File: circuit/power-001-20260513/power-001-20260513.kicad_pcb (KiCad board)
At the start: 2 copper layers, 68.4 x 46.4 mm, 46 parts, among them J2 +5V_{Line}, J3 Power, J4 Logic, J5 Sub_{Power}, J6 Sub_{Signal}, Q1 BSS138, Q2 PMOS, U1 OKL-T/6-W12N-C, U2 OKL-T/6-W12N-C, U3 AZ1084-3.3, U4 BP5293-33, U5 PIC12F683-xSN

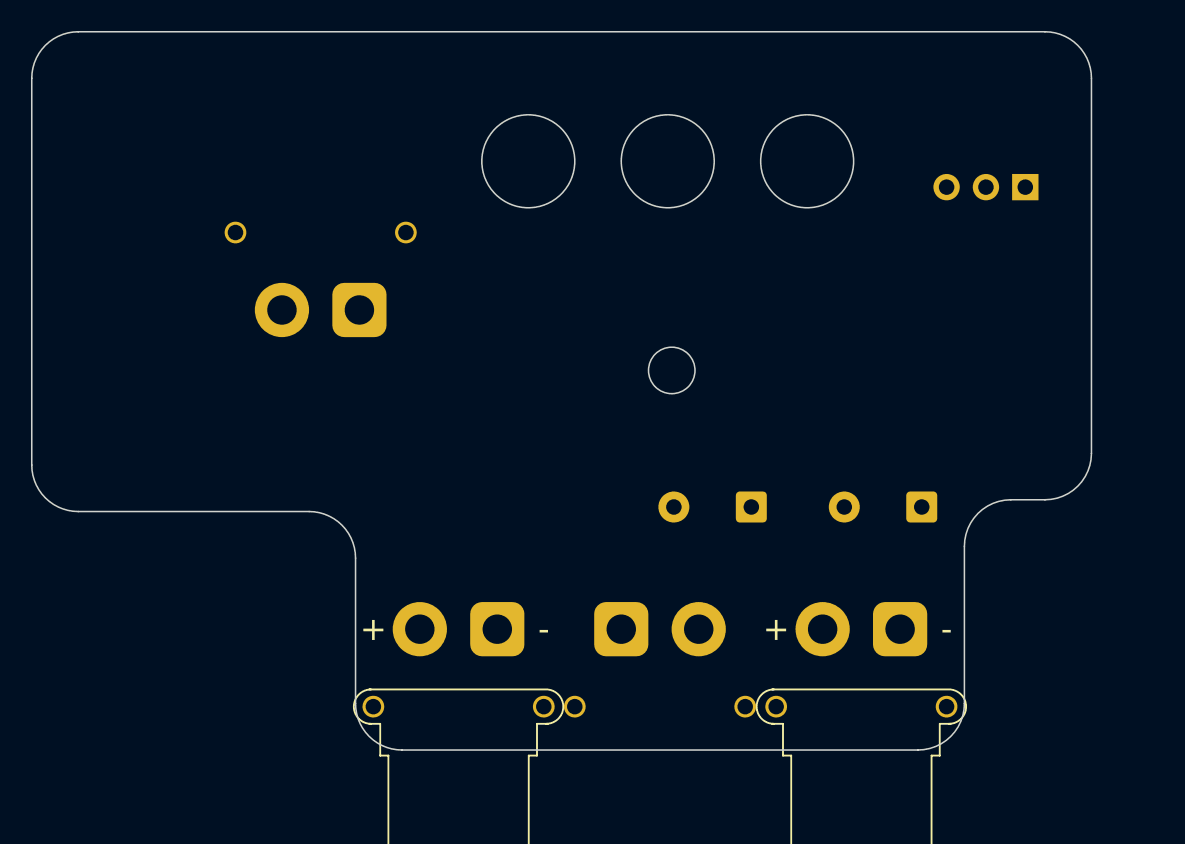
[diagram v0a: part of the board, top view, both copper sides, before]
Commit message: Update 電源基板のバッテリー接続口のフットプリントを作成＆紐づけ
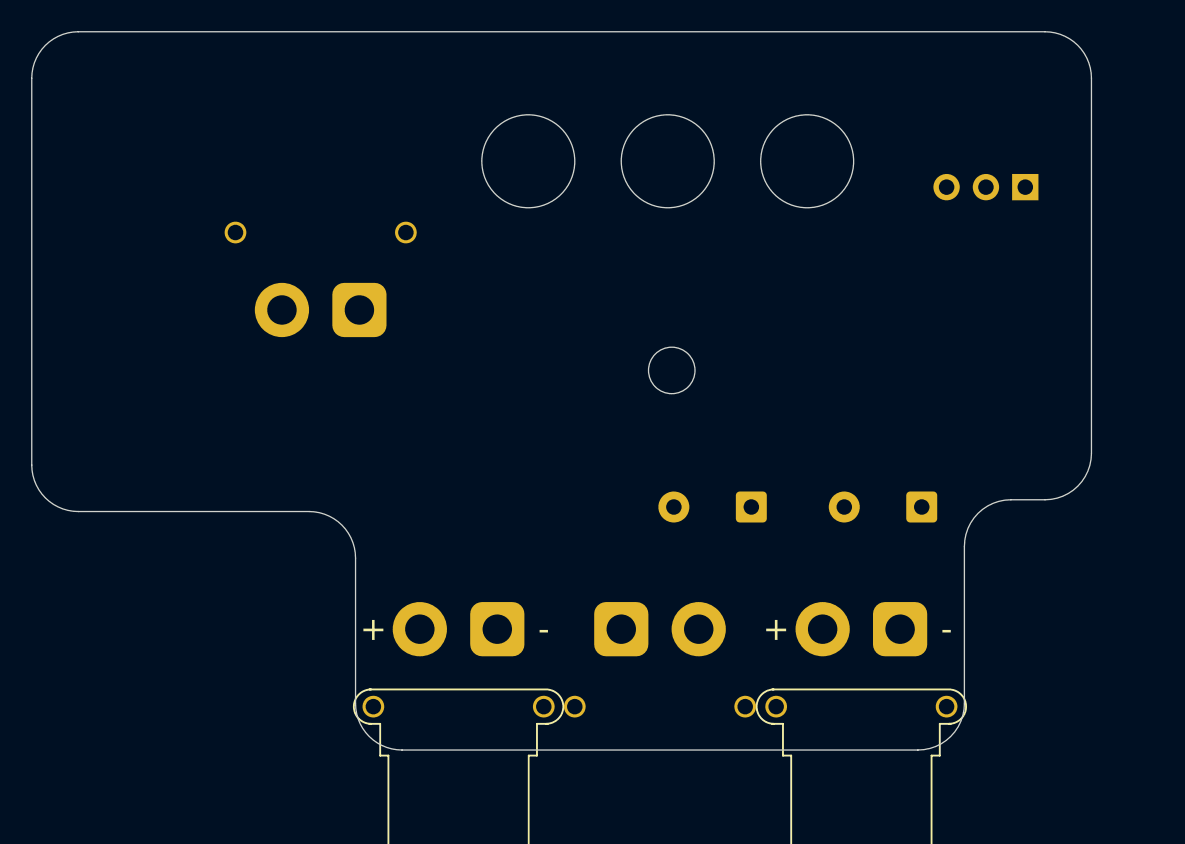
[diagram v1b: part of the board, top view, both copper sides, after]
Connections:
- J4 pad 1: +3.3V -> +5V
- J4 pad 2: +5V -> +3.3V

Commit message: Update 供給基板のXT30の向きを変更、それに伴う電源基板の回路図も変更
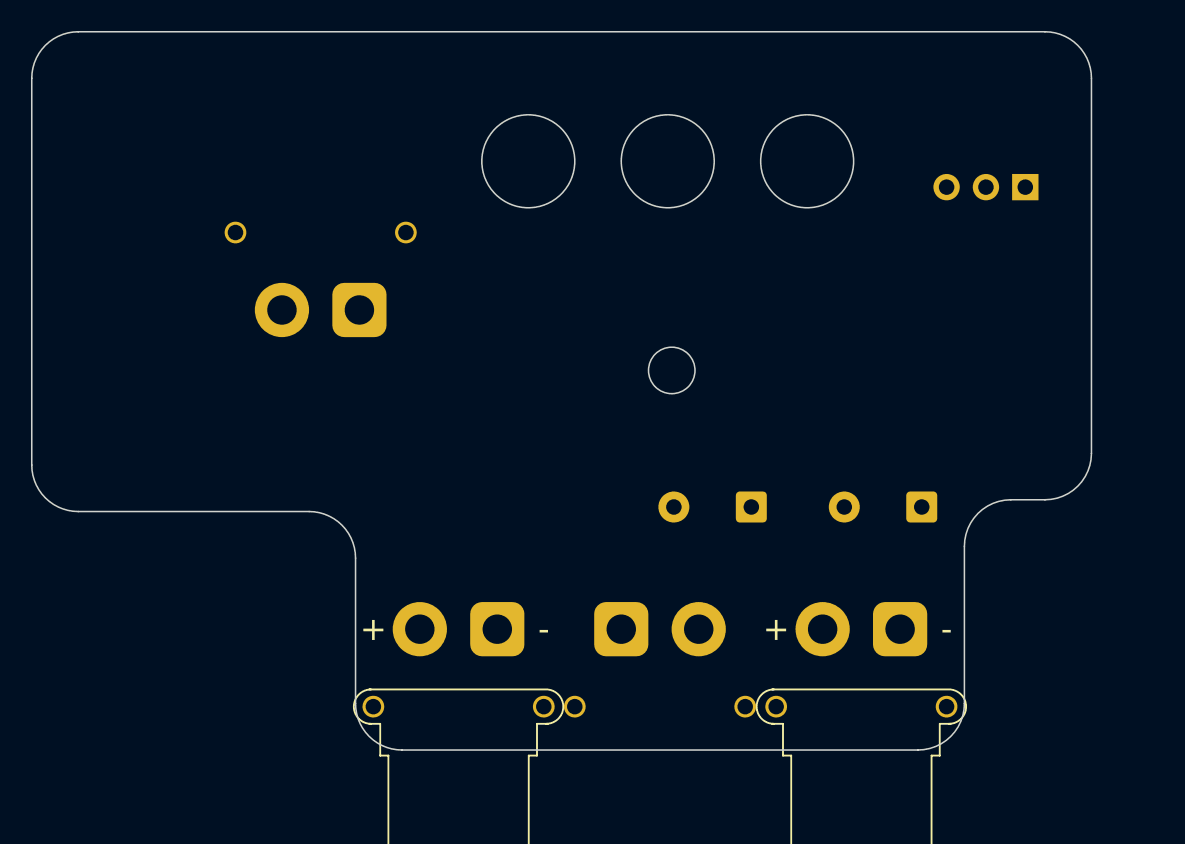
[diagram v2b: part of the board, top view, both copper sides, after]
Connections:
- J4 pad 1: +5V -> +3.3V
- J4 pad 2: +3.3V -> +5V
